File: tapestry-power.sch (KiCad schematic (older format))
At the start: 23 parts, among them J1 4.5-20V, J2 4.5-20V, J3 5V, J4 4.5-20V, J5 5V, U1 sic450

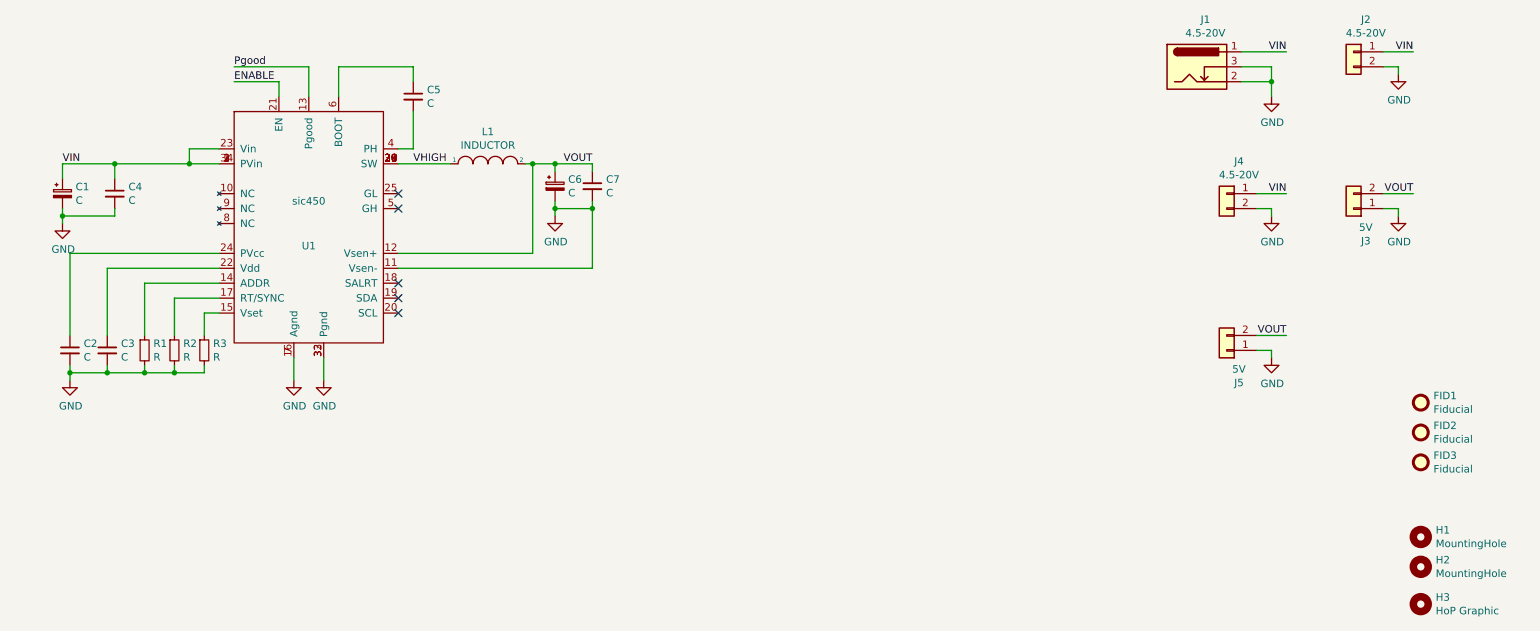
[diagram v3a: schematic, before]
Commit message: Updated board to wire in enable pin
And included some relevant resistor and capacitor values.
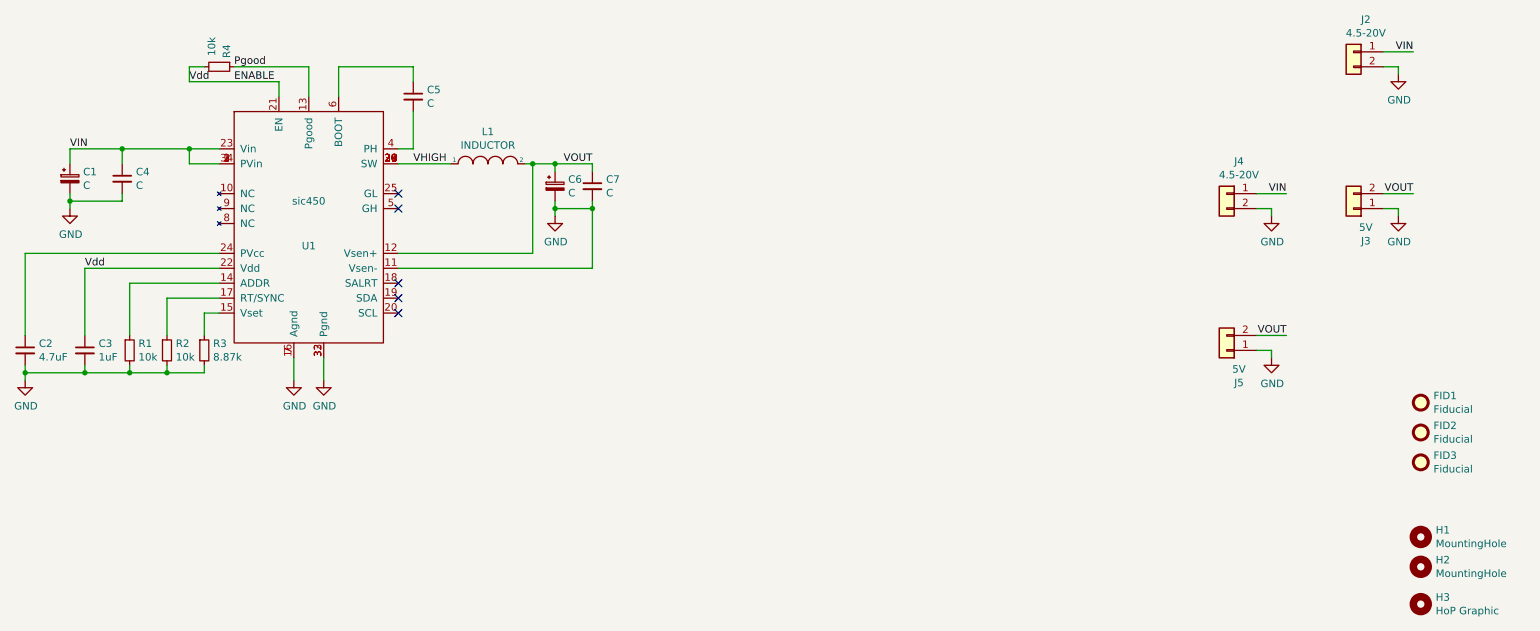
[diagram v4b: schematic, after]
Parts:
- removed J1: 4.5-20V, Connector_BarrelJack:BarrelJack_Horizontal, symbol Connector:Barrel_Jack_Switch
- added R4: 10k, Resistor_SMD:R_0805_2012Metric_Pad1.20x1.40mm_HandSolder, symbol Device:R_Small
- C2: value C -> 4.7uF
- C3: value C -> 1uF
- R1: value R -> 10k; Address (none) -> 14
- R2: value R -> 10k; Field4 (none) -> 10k sets PMBus sync to 1250 kHz
- R3: value R -> 8.87k; Voltage (none) -> 8.87k = 5V. 11k = 12V
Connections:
- net ENABLE: now also C3.1, U1.22 (Vdd), R4.2
- net Pgood: now also R4.1
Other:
- moved on the sheet: C1, C2, C3, C4, R1, R2
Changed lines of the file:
@@
 ENABLE
-Wire Wire Line
-	2100 1200 2400 1200
 Wire Wire Line
 	2400 1200 2400 1300
@@
 L power:GND #PWR0101
 U 1 1 60AF0485
-P 950 2150
-F 0 "#PWR0101" H 950 1900 50  0001 C CNN
-F 1 "GND" H 955 1977 50  0000 C CNN
-F 2 "" H 950 2150 50  0001 C CNN
-F 3 "" H 950 2150 50  0001 C CNN
-	1    950  2150
+P 1000 2050
+F 0 "#PWR0101" H 1000 1800 50  0001 C CNN
+F 1 "GND" H 1005 1877 50  0000 C CNN
+F 2 "" H 1000 2050 50  0001 C CNN
+F 3 "" H 1000 2050 50  0001 C CNN
+	1    1000 2050
 	1    0    0    -1
 $EndComp
@@
 L Device:C_Small C4
 U 1 1 60AF0B09
-P 1300 1950
-F 0 "C4" H 1392 1996 50  0000 L CNN
-F 1 "C" H 1392 1905 50  0000 L CNN
-F 2 "Capacitor_SMD:C_0805_2012Metric_Pad1.18x1.45mm_HandSolder" H 1300 1950 50  0001 C CNN
-F 3 "~" H 1300 1950 50  0001 C CNN
-	1    1300 1950
+P 1350 1850
+F 0 "C4" H 1442 1896 50  0000 L CNN
+F 1 "C" H 1442 1805 50  0000 L CNN
+F 2 "Capacitor_SMD:C_0805_2012Metric_Pad1.18x1.45mm_HandSolder" H 1350 1850 50  0001 C CNN
+F 3 "~" H 1350 1850 50  0001 C CNN
+	1    1350 1850
 	1    0    0    -1
 $EndComp
@@
 L Device:CP_Small C1
 U 1 1 60AF2034
-P 950 1950
-F 0 "C1" H 1038 1996 50  0000 L CNN
-F 1 "C" H 1038 1905 50  0000 L CNN
-F 2 "Capacitor_SMD:CP_Elec_4x5.3" H 950 1950 50  0001 C CNN
-F 3 "~" H 950 1950 50  0001 C CNN
-	1    950  1950
-	1    0    0    -1
-$EndComp
-Wire Wire Line
-	950  2150 950  2100
-Wire Wire Line
-	950  2100 1300 2100
-Wire Wire Line
-	1300 2100 1300 2050
-Wire Wire Line
-	950  2100 950  2050
-Connection ~ 950  2100
-Wire Wire Line
-	950  1850 950  1750
-Wire Wire Line
-	950  1750 1300 1750
-Wire Wire Line
-	1300 1850 1300 1750
-Connection ~ 1300 1750
-Wire Wire Line
-	1300 1750 1800 1750
+P 1000 1850
+F 0 "C1" H 1088 1896 50  0000 L CNN
+F 1 "C" H 1088 1805 50  0000 L CNN
+F 2 "Capacitor_SMD:CP_Elec_4x5.3" H 1000 1850 50  0001 C CNN
+F 3 "~" H 1000 1850 50  0001 C CNN
+	1    1000 1850
+	1    0    0    -1
+$EndComp
+Wire Wire Line
+	1000 2050 1000 2000
+Wire Wire Line
+	1000 2000 1350 2000
+Wire Wire Line
+	1350 2000 1350 1950
+Wire Wire Line
+	1000 2000 1000 1950
+Connection ~ 1000 2000
+Wire Wire Line
+	1000 1750 1000 1650
+Wire Wire Line
+	1000 1650 1350 1650
+Wire Wire Line
+	1350 1750 1350 1650
 Wire Wire Line
 	1800 1750 1800 1650
 Wire Wire Line
 	1800 1650 2000 1650
-Connection ~ 1800 1750
 Wire Wire Line
 	1800 1750 2000 1750
@@
 P 1900 3000
 F 0 "R3" H 1959 3046 50  0000 L CNN
-F 1 "R" H 1959 2955 50  0000 L CNN
+F 1 "8.87k" H 1959 2955 50  0000 L CNN
 F 2 "Resistor_SMD:R_0805_2012Metric_Pad1.20x1.40mm_HandSolder" H 1900 3000 50  0001 C CNN
 F 3 "~" H 1900 3000 50  0001 C CNN
+F 4 "8.87k = 5V.  11k = 12V" H 1900 3000 50  0001 C CNN "Voltage"
 	1    1900 3000
 	1    0    0    -1
@@
 L Device:R_Small R2
 U 1 1 60AF74AE
-P 1700 3000
-F 0 "R2" H 1759 3046 50  0000 L CNN
-F 1 "R" H 1759 2955 50  0000 L CNN
-F 2 "Resistor_SMD:R_0805_2012Metric_Pad1.20x1.40mm_HandSolder" H 1700 3000 50  0001 C CNN
-F 3 "~" H 1700 3000 50  0001 C CNN
-	1    1700 3000
+P 1650 3000
+F 0 "R2" H 1709 3046 50  0000 L CNN
+F 1 "10k" H 1709 2955 50  0000 L CNN
+F 2 "Resistor_SMD:R_0805_2012Metric_Pad1.20x1.40mm_HandSolder" H 1650 3000 50  0001 C CNN
+F 3 "~" H 1650 3000 50  0001 C CNN
+F 4 "10k sets PMBus sync to 1250 kHz" H 1650 3000 50  0001 C CNN "Field4"
+	1    1650 3000
 	1    0    0    -1
 $EndComp
@@
 L Device:R_Small R1
 U 1 1 60AF7685
-P 1500 3000
-F 0 "R1" H 1559 3046 50  0000 L CNN
-F 1 "R" H 1559 2955 50  0000 L CNN
-F 2 "Resistor_SMD:R_0805_2012Metric_Pad1.20x1.40mm_HandSolder" H 1500 3000 50  0001 C CNN
-F 3 "~" H 1500 3000 50  0001 C CNN
-	1    1500 3000
+P 1400 3000
+F 0 "R1" H 1459 3046 50  0000 L CNN
+F 1 "10k" H 1459 2955 50  0000 L CNN
+F 2 "Resistor_SMD:R_0805_2012Metric_Pad1.20x1.40mm_HandSolder" H 1400 3000 50  0001 C CNN
+F 3 "~" H 1400 3000 50  0001 C CNN
+F 4 "14" H 1400 3000 50  0001 C CNN "Address"
+	1    1400 3000
 	1    0    0    -1
 $EndComp
@@
 L Device:C_Small C3
 U 1 1 60AF7838
-P 1250 3000
-F 0 "C3" H 1342 3046 50  0000 L CNN
-F 1 "C" H 1342 2955 50  0000 L CNN
-F 2 "Capacitor_SMD:C_0805_2012Metric_Pad1.18x1.45mm_HandSolder" H 1250 3000 50  0001 C CNN
-F 3 "~" H 1250 3000 50  0001 C CNN
-	1    1250 3000
+P 1100 3000
+F 0 "C3" H 1192 3046 50  0000 L CNN
+F 1 "1uF" H 1192 2955 50  0000 L CNN
+F 2 "Capacitor_SMD:C_0805_2012Metric_Pad1.18x1.45mm_HandSolder" H 1100 3000 50  0001 C CNN
+F 3 "~" H 1100 3000 50  0001 C CNN
+	1    1100 3000
 	1    0    0    -1
 $EndComp
@@
 L Device:C_Small C2
 U 1 1 60AF7FEC
-P 1000 3000
-F 0 "C2" H 1092 3046 50  0000 L CNN
-F 1 "C" H 1092 2955 50  0000 L CNN
-F 2 "Capacitor_SMD:C_0805_2012Metric_Pad1.18x1.45mm_HandSolder" H 1000 3000 50  0001 C CNN
-F 3 "~" H 1000 3000 50  0001 C CNN
-	1    1000 3000
+P 700 3000
+F 0 "C2" H 792 3046 50  0000 L CNN
+F 1 "4.7uF" H 792 2955 50  0000 L CNN
+F 2 "Capacitor_SMD:C_0805_2012Metric_Pad1.18x1.45mm_HandSolder" H 700 3000 50  0001 C CNN
+F 3 "~" H 700 3000 50  0001 C CNN
+	1    700  3000
 	1    0    0    -1
 $EndComp
@@
 L power:GND #PWR0104
 U 1 1 60AF8224
-P 1000 3200
-F 0 "#PWR0104" H 1000 2950 50  0001 C CNN
-F 1 "GND" H 1005 3027 50  0000 C CNN
-F 2 "" H 1000 3200 50  0001 C CNN
-F 3 "" H 1000 3200 50  0001 C CNN
-	1    1000 3200
-	1    0    0    -1
-$EndComp
-Wire Wire Line
-	1000 3200 1000 3150
-Wire Wire Line
-	1250 3100 1250 3150
-Wire Wire Line
-	1250 3150 1000 3150
-Connection ~ 1000 3150
-Wire Wire Line
-	1000 3150 1000 3100
+P 700 3200
+F 0 "#PWR0104" H 700 2950 50  0001 C CNN
+F 1 "GND" H 705 3027 50  0000 C CNN
+F 2 "" H 700 3200 50  0001 C CNN
+F 3 "" H 700 3200 50  0001 C CNN
+	1    700  3200
+	1    0    0    -1
+$EndComp
+Wire Wire Line
+	700  3200 700  3150
+Wire Wire Line
+	1100 3100 1100 3150
+Wire Wire Line
+	1100 3150 700  3150
+Connection ~ 700  3150
+Wire Wire Line
+	700  3150 700  3100
 Wire Wire Line
 	1900 3100 1900 3150
 Wire Wire Line
-	1900 3150 1700 3150
-Connection ~ 1250 3150
-Wire Wire Line
-	1500 3100 1500 3150
-Connection ~ 1500 3150
-Wire Wire Line
-	1500 3150 1250 3150
-Wire Wire Line
-	1700 3100 1700 3150
-Connection ~ 1700 3150
-Wire Wire Line
-	1700 3150 1500 3150
+	1900 3150 1650 3150
+Wire Wire Line
+	1400 3100 1400 3150
+Wire Wire Line
+	1400 3150 1100 3150
+Wire Wire Line
+	1650 3100 1650 3150
+Wire Wire Line
+	1650 3150 1400 3150
 Wire Wire Line
 	1900 2900 1900 2750
@@
 	1900 2750 2000 2750
 Wire Wire Line
-	2000 2650 1700 2650
-Wire Wire Line
-	1700 2650 1700 2900
-Wire Wire Line
-	1500 2900 1500 2550
-Wire Wire Line
-	1500 2550 2000 2550
-Wire Wire Line
-	2000 2450 1250 2450
-Wire Wire Line
-	1250 2450 1250 2900
-Wire Wire Line
-	1000 2900 1000 2350
-Wire Wire Line
-	1000 2350 2000 2350
+	2000 2650 1650 2650
+Wire Wire Line
+	1650 2650 1650 2900
+Wire Wire Line
+	1400 2900 1400 2550
+Wire Wire Line
+	1400 2550 2000 2550
+Wire Wire Line
+	2000 2450 1100 2450
+Wire Wire Line
+	700  2900 700  2350
+Wire Wire Line
+	700  2350 2000 2350
 NoConn ~ 3200 1950
 NoConn ~ 3200 2050
@@
 NoConn ~ 3200 2650
 NoConn ~ 3200 2750
-Text Label 950  1750 0    50   ~ 0
+Text Label 1000 1650 0    50   ~ 0
 VIN
 $Comp
@@
 Text Label 4500 1750 2    50   ~ 0
 VOUT
-$Comp
-L Connector:Barrel_Jack_Switch J1
-U 1 1 60BA06F1
-P 8550 1100
-F 0 "J1" H 8607 1417 50  0000 C CNN
-F 1 "4.5-20V" H 8607 1326 50  0000 C CNN
-F 2 "Connector_BarrelJack:BarrelJack_Horizontal" H 8600 1060 50  0001 C CNN
-F 3 "~" H 8600 1060 50  0001 C CNN
-	1    8550 1100
-	1    0    0    -1
-$EndComp
 $Comp
 L Connector_Generic:Conn_01x02 J2
@@
 	-1   0    0    -1
 $EndComp
-Text Label 9150 1000 2    50   ~ 0
-VIN
-$Comp
-L power:GND #PWR0106
-U 1 1 60BA4363
-P 9050 1300
-F 0 "#PWR0106" H 9050 1050 50  0001 C CNN
-F 1 "GND" H 9055 1127 50  0000 C CNN
-F 2 "" H 9050 1300 50  0001 C CNN
-F 3 "" H 9050 1300 50  0001 C CNN
-	1    9050 1300
-	1    0    0    -1
-$EndComp
 Text Label 10000 1950 2    50   ~ 0
 VOUT
-Wire Wire Line
-	8850 1000 9150 1000
-Wire Wire Line
-	8850 1100 9050 1100
-Wire Wire Line
-	9050 1100 9050 1200
-Wire Wire Line
-	8850 1200 9050 1200
-Connection ~ 9050 1200
-Wire Wire Line
-	9050 1200 9050 1300
 Text Label 10000 1000 2    50   ~ 0
 VIN
@@
 Wire Wire Line
 	9050 3000 8950 3000
+Wire Wire Line
+	1800 1650 1350 1650
+Connection ~ 1800 1650
+Connection ~ 1350 1650
+Connection ~ 1100 3150
+Connection ~ 1400 3150
+Connection ~ 1650 3150
+$Comp
+L Device:R_Small R4
+U 1 1 60FBACA8
+P 2000 1100
+F 0 "R4" H 1850 1150 50  0000 L CNN
+F 1 "10k" H 1800 1050 50  0000 L CNN
+F 2 "Resistor_SMD:R_0805_2012Metric_Pad1.20x1.40mm_HandSolder" H 2000 1100 50  0001 C CNN
+F 3 "~" H 2000 1100 50  0001 C CNN
+F 4 "14" H 2000 1100 50  0001 C CNN "Address"
+	1    2000 1100
+	0    1    1    0
+$EndComp
+Text Label 1100 2450 0    50   ~ 0
+Vdd
+Wire Wire Line
+	1100 2450 1100 2900
+Wire Wire Line
+	1900 1100 1800 1100
+Wire Wire Line
+	1800 1100 1800 1200
+Wire Wire Line
+	1800 1200 2400 1200
+Text Label 1800 1200 0    50   ~ 0
+Vdd
 $EndSCHEMATC
